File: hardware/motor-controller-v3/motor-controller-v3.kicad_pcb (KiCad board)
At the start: 4 copper layers, 50 x 100 mm, 123 parts, among them J101 WAGO, J102 WAGO, J103 2.54mm R/A, J104 WAGO, J105 WAGO, J106 WAGO, Q101 AO3401A, Q102 AO3401A, Q103 AO3401A, Q104 AO3400A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

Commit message: Finished motor-controller-v3 draft
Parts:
- H101, H102, H103, H104: value M3 -> M2.5; footprint MountingHole:MountingHole_3.2mm_M3_Pad_Via -> MountingHole:MountingHole_2.7mm_M2.5_Pad_Via
- H105, H106: value M2.5 -> M2; footprint MountingHole:MountingHole_2.7mm_M2.5_Pad_Via -> MountingHole:MountingHole_2.2mm_M2_Pad_Via
- R106, R109, R111: value 4.7kΩ -> 130Ω
- R113: value 4.7kΩ -> 56Ω
- moved TP121 99.5 mm to (223.7, 128.2)
- moved TP120 94.9 mm to (223.7, 135.8)
- moved TP113 94.3 mm to (199.0, 140.1)
- moved TP114 88.9 mm to (196.9, 138.7)
- moved TP115 83.4 mm to (195.0, 137.0)
- moved TP103 83.1 mm to (193.0, 140.0)
- moved TP109 76.1 mm to (196.0, 123.1)
- moved TP118 75.6 mm to (223.7, 101.7)
- moved TP119 69.3 mm to (223.7, 94.2)
- moved TP126 67.6 mm to (196.0, 119.5)
- moved TP110 62.3 mm to (200.0, 110.0)
- moved TP107 61.7 mm to (196.0, 116.2)
- moved TP117 59.9 mm to (223.7, 60.2)
- moved TP101 56.2 mm to (223.7, 84.7)
- moved TP111 56.0 mm to (198.4, 107.3)
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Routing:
- net +3.3V: track 0.00 -> 116.7 mm, vias 0 -> 9
- net /~{MOTOR_FAULT}: track 0.00 -> 95.5 mm, vias 0 -> 4
- net /~{MOTOR_SLEEP}: track 0.00 -> 87.8 mm, vias 0 -> 3
- net /~{MOTOR_CHOPPING}: track 0.00 -> 87.1 mm, vias 0 -> 4
- net /~{TEMP_ALRT}: track 0.00 -> 82.0 mm, vias 0 -> 4
- net /STEERING_MOTOR_DIR: track 0.00 -> 55.0 mm, vias 0 -> 1
- net /STEERING_MOTOR_PWM: track 0.00 -> 54.1 mm, vias 0 -> 1
- net /DC Motor Controller - Rear Wheels/GH2: track 0.00 -> 31.0 mm
- net /TEMP_SDA: track 0.00 -> 30.7 mm, vias 0 -> 1
- net /REAR_MOTOR_OUT_B: track 0.00 -> 30.5 mm
- net /TEMP_SCL: track 0.00 -> 28.8 mm, vias 0 -> 1
- net /DC Motor Controller - Rear Wheels/GL2: track 0.00 -> 27.5 mm
- net /FRONT_MOTOR_PWM: track 0.00 -> 26.7 mm, vias 0 -> 1
- net /DC Motor Controller - Front Wheels/GH2: track 0.00 -> 26.4 mm
- net /FRONT_MOTOR_OUT_B: track 0.00 -> 26.2 mm
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- added copper zone on B.Cu, net +3.3V
- added copper zone on F.Cu, net +3.3V
- added copper zone on B.Cu, net +BATT
- added copper zone on F.Cu, net +BATT
- added copper zone on In2.Cu, net +BATT
- added copper zone on F.Cu, net /DC Motor Controller - Front Wheels/V_SENSE
- added copper zone on F.Cu, net /DC Motor Controller - Rear Wheels/V_SENSE
- added copper zone on F.Cu, net /DC Motor Controller - Steering/V_SENSE
- added copper zone on F.Cu, net /FRONT_MOTOR_OUT_A
- added copper zone on F.Cu, net /FRONT_MOTOR_OUT_B
- added copper zone on F.Cu, net /REAR_MOTOR_OUT_A
- added copper zone on F.Cu, net /REAR_MOTOR_OUT_B
- added copper zone on F.Cu, net /STEERING_MOTOR_OUT_A
- added copper zone on F.Cu, net /STEERING_MOTOR_OUT_B
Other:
- board text added: "+3V3"
- board text added: "0 mm"
- board text added: "0.01524 mm"
- board text added: "0.07112 mm"
- board text added: "0.2000 mm / 0.2000 mm"
- board text added: "0.21082 mm"
- board text added: "0.2997 mm"
- board text added: "1.0668 mm"
- board text added: "1.6916 mm"
- board text added: "50.0000 mm x 100.0000 mm"
- board text added: "BATT+"
- board text added: "Fabrication Notes"
- board text added: "GND"
- board text added: "Geeks for Kids DC Motor Controller V3 - October 2025"
- board text added: "IN1A"
- board text added: "IN1B"
- board text added: "IN2A"
- board text added: "IN2B"
- board text added: "IN3A"
- board text added: "IN3B"
- board text added: "OUT1A"
- board text added: "OUT1B"
- board text added: "OUT2A"
- board text added: "OUT2B"
- board text added: "OUT3A"
- board text added: "OUT3B"
- board text added: "SCL"
- board text added: "SDA"
- board text added: "Thickness (mm)"
- board text added: "~{ALRT}"
- board text added: "~{FAULT}"
- board text added: "~{SLP}"
- board text removed: "0 in"
- board text removed: "0.0006 in"
- board text removed: "0.0028 in"
- board text removed: "0.0079 in / 0.0079 in"
- board text removed: "0.0083 in"
- board text removed: "0.0118 in"
- board text removed: "0.042 in"
- board text removed: "0.0666 in"
- board text removed: "1.9685 in x 3.9370 in"
- board text removed: "Design Notes"
- board text removed: "Thickness (inches)"

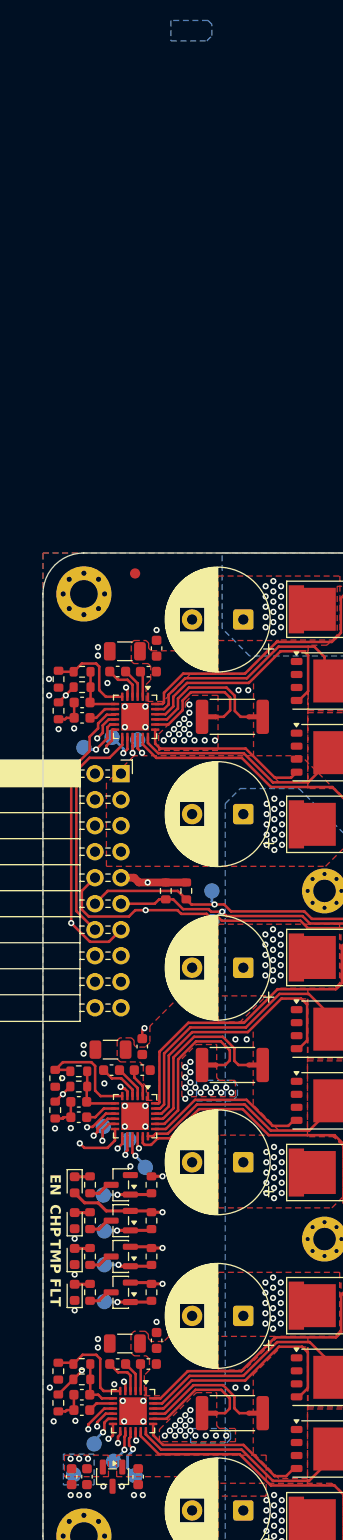
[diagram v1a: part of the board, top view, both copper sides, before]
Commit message: Adjust R_sense
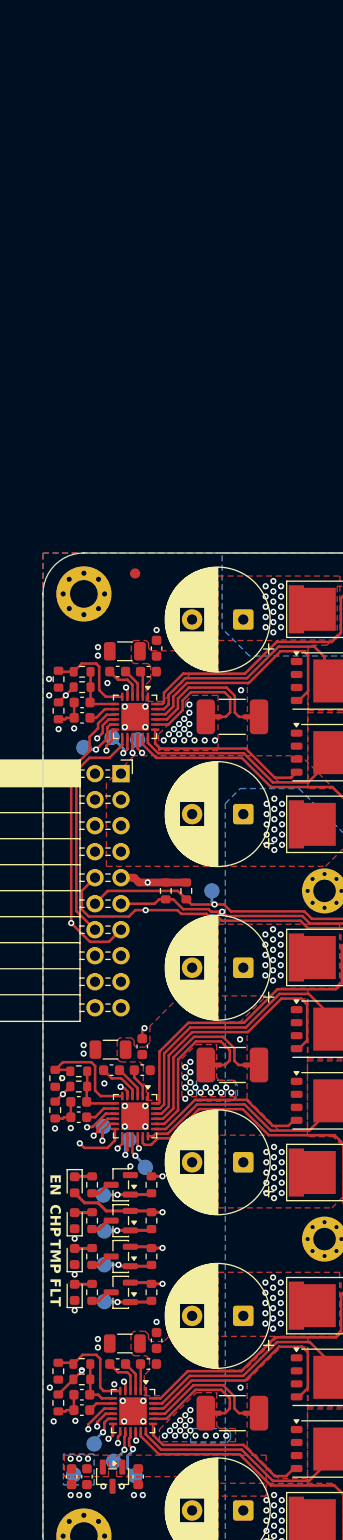
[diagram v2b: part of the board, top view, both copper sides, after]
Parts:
- R201, R301, R401: value 4.7kΩ -> 2.7kΩ
- R202, R302, R402: value 1kΩ -> 4.7kΩ
- R206, R306, R406: value 1mΩ -> 5mΩ; footprint Resistor_SMD:R_2512_6332Metric -> motor-controller-v3:DSLR-M_K-3
- moved NT201 0.40 mm to (210.2, 66.0)
- moved NT202 0.40 mm to (206.8, 66.0)
- moved NT301 0.40 mm to (210.2, 100.0)
- moved NT302 0.40 mm to (206.8, 100.0)
- moved NT401 0.40 mm to (210.2, 134.0)
- moved NT402 0.40 mm to (206.8, 134.0)
- moved R106 0.20 mm to (194.8, 115.2)
- moved R109 0.20 mm to (194.8, 118.7)
- moved R111 0.20 mm to (194.8, 122.2)
- moved R113 0.20 mm to (194.8, 111.7)
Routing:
- net GND: track 17.9 -> 17.8 mm, vias 107 -> 104
